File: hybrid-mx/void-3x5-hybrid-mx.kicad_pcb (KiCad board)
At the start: 2 copper layers, 140.5 x 112.5 mm, 81 parts, among them J1 Conn_01x02, J2 Conn_01x03_MountingPin, J3 Conn_01x02

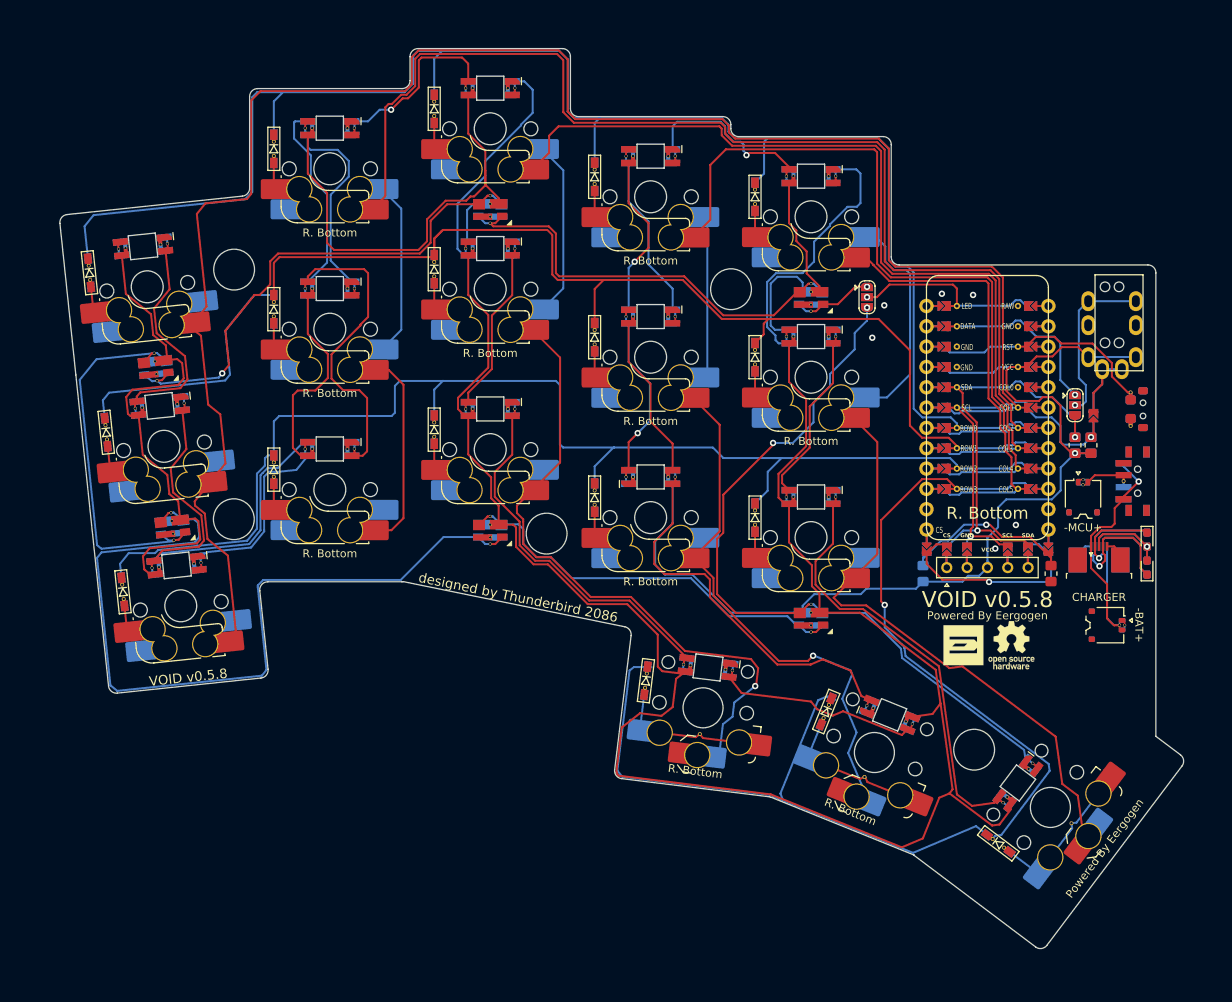
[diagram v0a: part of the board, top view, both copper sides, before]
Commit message: added choc
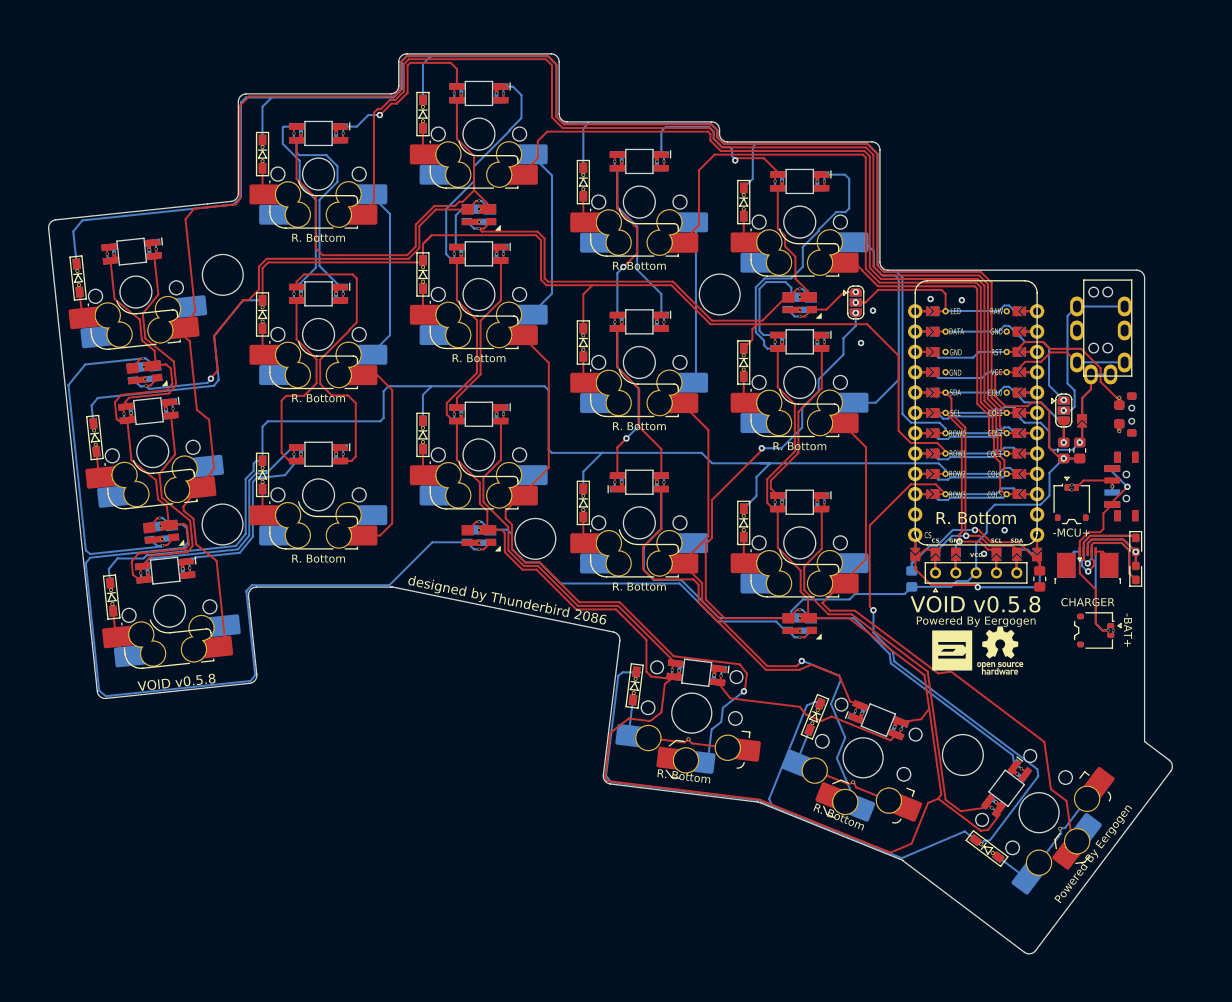
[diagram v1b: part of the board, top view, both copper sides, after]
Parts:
- moved D6 1.56 mm to (107.6, 52.8)
- moved JP1 1.56 mm to (181.8, 71.4)
- moved L12 1.56 mm to (154.7, 53.7)
- moved LED1 1.56 mm to (216.8, 105.2)
- moved LED2 1.56 mm to (216.8, 101.7)
- moved LED3 1.56 mm to (216.8, 105.2)
- moved LED4 1.56 mm to (216.8, 101.7)
- moved S4 1.56 mm to (114.6, 95.4)
- moved JP2 1.56 mm to (207.8, 84.9)
- moved S3 1.56 mm to (91.8, 70.1)
- moved DISP1 1.56 mm to (196.8, 85.2)
- moved LOGO2 1.56 mm to (199.8, 114.9)
- moved MCU1 1.56 mm to (196.8, 85.2)
- moved L17 1.56 mm to (184.6, 123.6)
- moved L23 1.56 mm to (134.7, 100.5)
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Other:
- outline, holes or cut-outs redrawn

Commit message: added holes for oled window
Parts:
- moved LOGO1 3.00 mm to (196.8, 114.9)
- moved LOGO2 3.00 mm to (202.8, 114.9)
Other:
- outline, holes or cut-outs redrawn
- board text added: "VOID v0.5.9"
- board text removed: "VOID v0.5.8"

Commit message: Mcu cover (#7)
* more plates

* updated workflow

* mcu cover

* small change
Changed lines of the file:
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@@
 		(fp_arc
 			(start 4.085177 -6.750222)
-			(mid 5.499395 -6.164435)
+			(mid 5.499391 -6.164435)
 			(end 6.085176 -4.750218)
 			(stroke
@@
 		(fp_arc
 			(start 4.085177 -6.750222)
-			(mid 5.499395 -6.164435)
+			(mid 5.499391 -6.164435)
 			(end 6.085176 -4.750218)
 			(stroke
@@
 		(fp_arc
 			(start 4.085176 -6.750219)
-			(mid 5.499391 -6.164436)
+			(mid 5.499388 -6.164435)
 			(end 6.085177 -4.750222)
 			(stroke
@@
 		(fp_arc
 			(start 4.085176 -6.750219)
-			(mid 5.499391 -6.164436)
+			(mid 5.499388 -6.164435)
 			(end 6.085177 -4.750222)
 			(stroke
@@
 		(fp_arc
 			(start 4.085177 -6.750222)
-			(mid 5.499395 -6.164435)
+			(mid 5.499391 -6.164435)
 			(end 6.085176 -4.750218)
 			(stroke
@@
 		(fp_arc
 			(start 4.085177 -6.750222)
-			(mid 5.499395 -6.164435)
+			(mid 5.499391 -6.164435)
 			(end 6.085176 -4.750218)
 			(stroke
@@
 		(fp_arc
 			(start 4.085177 -6.750222)
-			(mid 5.499395 -6.164435)
+			(mid 5.499391 -6.164435)
 			(end 6.085176 -4.750218)
 			(stroke
@@
 		(fp_arc
 			(start 4.085177 -6.750222)
-			(mid 5.499395 -6.164435)
+			(mid 5.499391 -6.164435)
 			(end 6.085176 -4.750218)
 			(stroke
@@
 		(fp_arc
 			(start 4.085177 -6.750222)
-			(mid 5.499395 -6.164435)
+			(mid 5.499391 -6.164435)
 			(end 6.085176 -4.750218)
 			(stroke
@@
 		(fp_arc
 			(start 4.085177 -6.750222)
-			(mid 5.499395 -6.164435)
+			(mid 5.499391 -6.164435)
 			(end 6.085176 -4.750218)
 			(stroke
@@
 		(fp_arc
 			(start 4.085177 -6.750222)
-			(mid 5.499395 -6.164435)
+			(mid 5.499391 -6.164435)
 			(end 6.085176 -4.750218)
 			(stroke
@@
 		(fp_arc
 			(start 4.085177 -6.750222)
-			(mid 5.499395 -6.164435)
+			(mid 5.499391 -6.164435)
 			(end 6.085176 -4.750218)
 			(stroke
@@
 		(fp_arc
 			(start 4.085177 -6.750222)
-			(mid 5.499395 -6.164435)
+			(mid 5.499391 -6.164435)
 			(end 6.085176 -4.750218)
 			(stroke
@@
 		(fp_arc
 			(start 4.085177 -6.750222)
-			(mid 5.499395 -6.164435)
+			(mid 5.499391 -6.164435)
 			(end 6.085176 -4.750218)
 			(stroke
@@
 		(fp_arc
 			(start 4.085177 -6.750222)
-			(mid 5.499395 -6.164435)
+			(mid 5.499391 -6.164435)
 			(end 6.085176 -4.750218)
 			(stroke
@@
 		(fp_arc
 			(start 4.085177 -6.750222)
-			(mid 5.499395 -6.164435)
+			(mid 5.499391 -6.164435)
 			(end 6.085176 -4.750218)
 			(stroke
@@
 		(fp_arc
 			(start 4.085176 -6.750219)
-			(mid 5.499391 -6.164436)
+			(mid 5.499388 -6.164435)
 			(end 6.085177 -4.750222)
 			(stroke
@@
 		(fp_arc
 			(start 4.085176 -6.750219)
-			(mid 5.499391 -6.164436)
+			(mid 5.499388 -6.164435)
 			(end 6.085177 -4.750222)
 			(stroke
@@
 		(fp_arc
 			(start 4.085177 -6.750222)
-			(mid 5.499395 -6.164435)
+			(mid 5.499391 -6.164435)
 			(end 6.085176 -4.750218)
 			(stroke
@@
 		(fp_arc
 			(start 4.085177 -6.750222)
-			(mid 5.499395 -6.164435)
+			(mid 5.499391 -6.164435)
 			(end 6.085176 -4.750218)
 			(stroke
@@
 		(fp_arc
 			(start 4.085176 -6.750219)
-			(mid 5.499391 -6.164436)
+			(mid 5.499388 -6.164435)
 			(end 6.085177 -4.750222)
 			(stroke
@@
 		(fp_arc
 			(start 4.085176 -6.750219)
-			(mid 5.499391 -6.164436)
+			(mid 5.499388 -6.164435)
 			(end 6.085177 -4.750222)
 			(stroke
@@
 		(fp_arc
 			(start 4.085177 -6.750222)
-			(mid 5.499395 -6.164435)
+			(mid 5.499391 -6.164435)
 			(end 6.085176 -4.750218)
 			(stroke
@@
 		(fp_arc
 			(start 4.085177 -6.750222)
-			(mid 5.499395 -6.164435)
+			(mid 5.499391 -6.164435)
 			(end 6.085176 -4.750218)
 			(stroke
@@
 		(fp_arc
 			(start 4.085177 -6.750222)
-			(mid 5.499395 -6.164435)
+			(mid 5.499391 -6.164435)
 			(end 6.085176 -4.750218)
 			(stroke
@@
 		(fp_arc
 			(start 4.085177 -6.750222)
-			(mid 5.499395 -6.164435)
+			(mid 5.499391 -6.164435)
 			(end 6.085176 -4.750218)
 			(stroke
@@
 		(fp_arc
 			(start 4.085177 -6.750222)
-			(mid 5.499395 -6.164435)
+			(mid 5.499391 -6.164435)
 			(end 6.085176 -4.750218)
 			(stroke
@@
 		(fp_arc
 			(start 4.085177 -6.750222)
-			(mid 5.499395 -6.164435)
+			(mid 5.499391 -6.164435)
 			(end 6.085176 -4.750218)
 			(stroke
@@
 		(fp_arc
 			(start 4.085177 -6.750222)
-			(mid 5.499395 -6.164435)
+			(mid 5.499391 -6.164435)
 			(end 6.085176 -4.750218)
 			(stroke
@@
 		(fp_arc
 			(start 4.085177 -6.750222)
-			(mid 5.499395 -6.164435)
+			(mid 5.499391 -6.164435)
 			(end 6.085176 -4.750218)
 			(stroke

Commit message: fixed bridge for hybrid-mx
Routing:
- net row_thumb: track 160.7 -> 157.2 mm

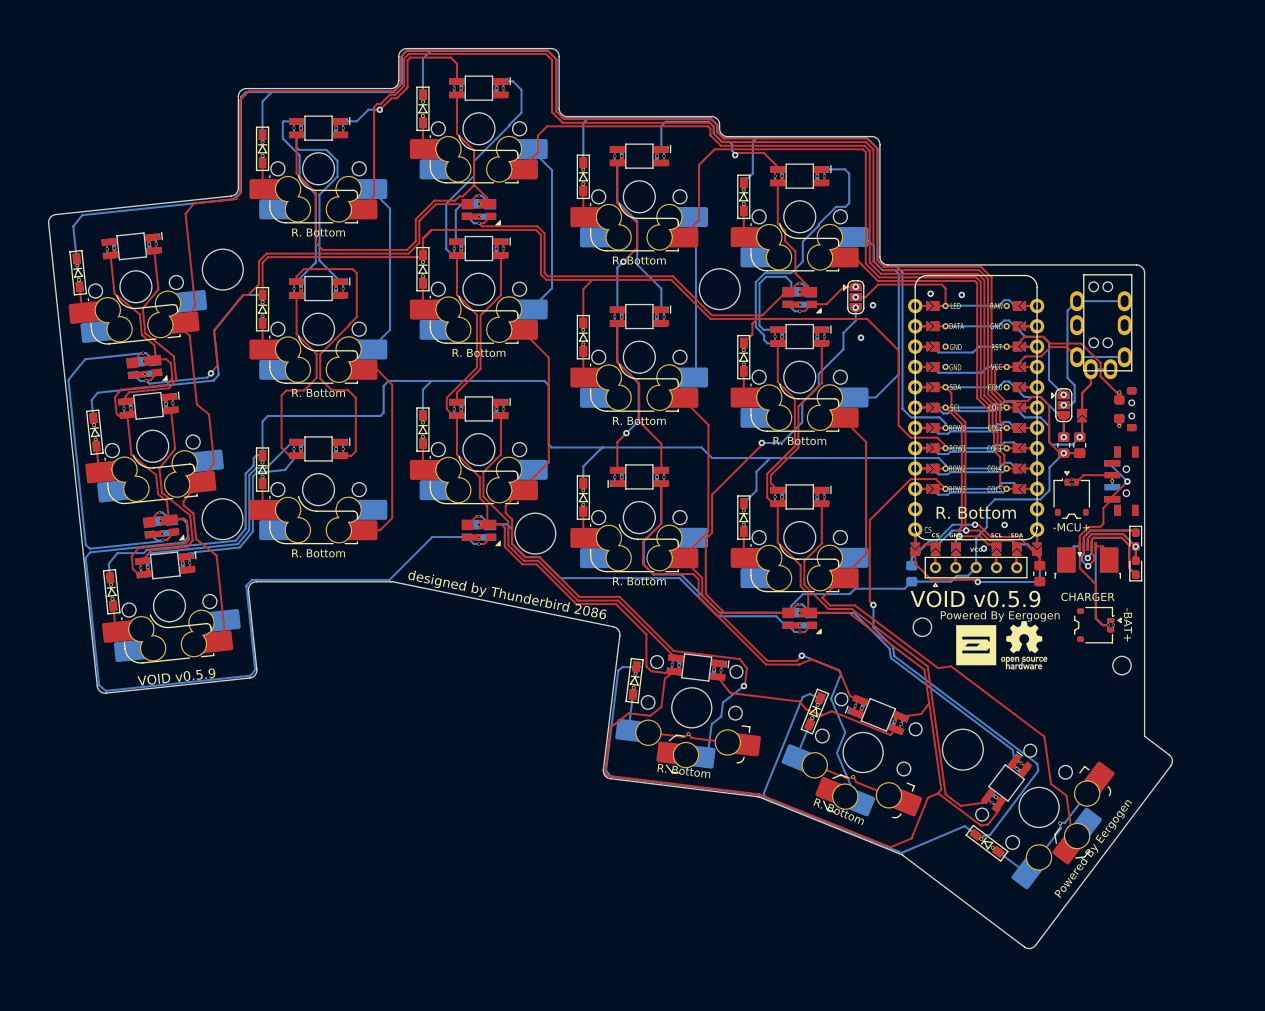
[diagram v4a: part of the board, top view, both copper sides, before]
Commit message: Changed TRRS to USB-C connector (#14)
* usb-c mod for hybrid

* updated
  - submodule
  - ergogen yaml
  - schematic and pcb

* updated cherry-mx

usb-c for communication between left and right hand sides

* updated choc

* updated choc

* fixed corner

* void-choc

* ergogen
  - bottom plate
  - charger plate

* updated choc

* updated ergogen

* cherry-mx
* hybrid-mx

* updated ergogen for VOID Choc

* refreshed submodule

* updated ergogen yaml

* updated PCBs

* updated version
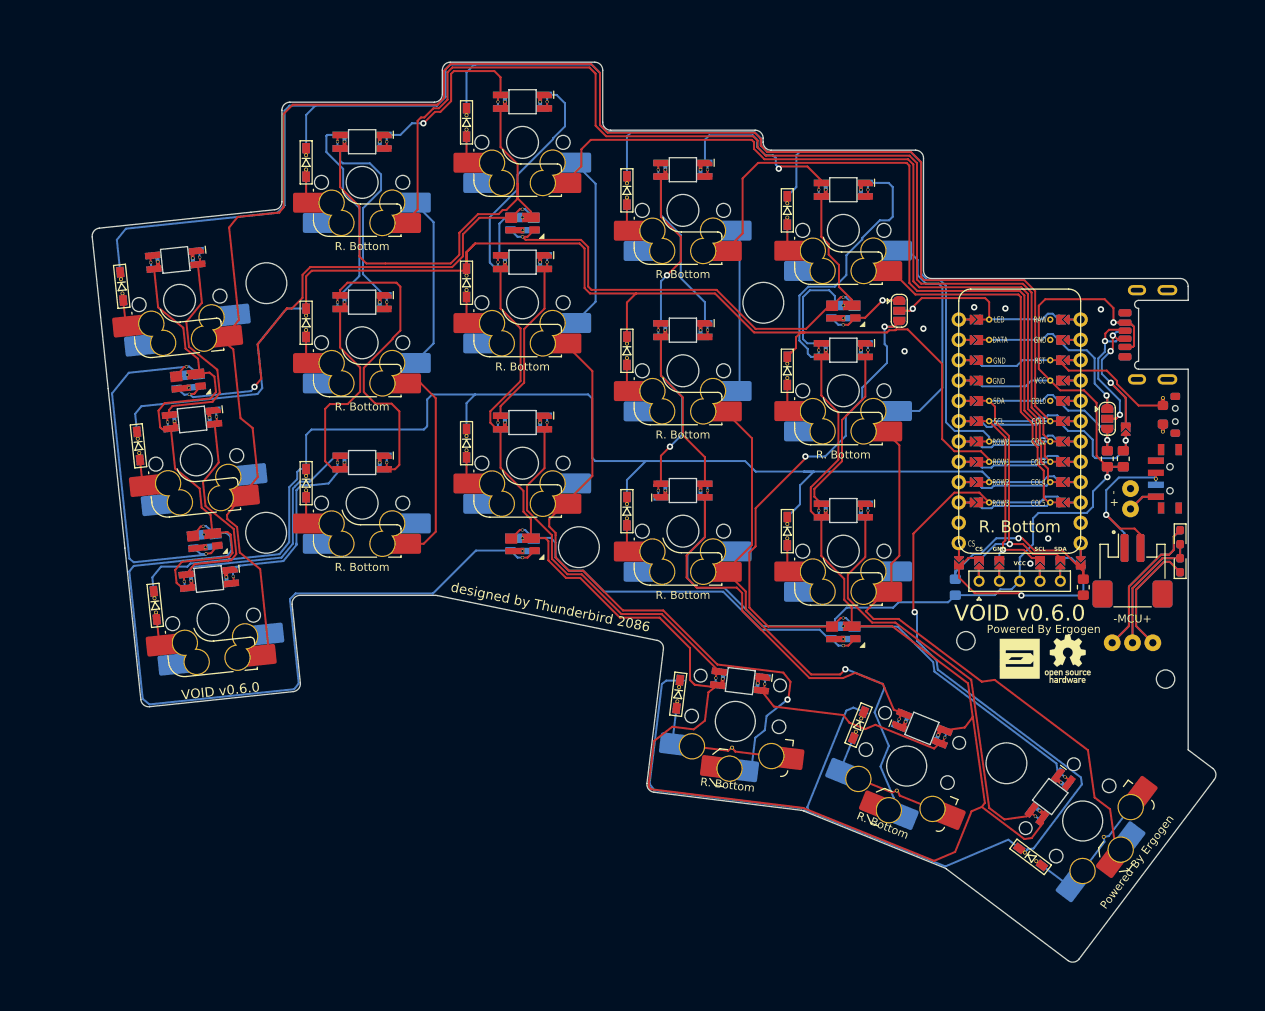
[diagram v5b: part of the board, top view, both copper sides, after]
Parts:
- removed TRRS1: MJ-4PP-9, TB2086_MISC:TRRS-PJ-320A-rev
- added J4: Conn_01x03, TB2086_MISC:Pogopin_1x03_P2.54mm, F.Cu at (216.3, 114.6)
- added SW_SPDT2: SW_SPDT2, TB2086_SMD:SW_SPDT_PCM12, F.Cu at (220.7, 94.1)
- J1: value Conn_01x02 -> USB_C_Receptacle_PowerOnly_6P; footprint TB2086_MISC:Molex_Pico-EZmate_78171-0002_1x02-1MP_P1.20mm_Vertical_rev -> TB2086_SMD:USB-20C-F-6C16_rev
- J2: value Conn_01x03_MountingPin -> Conn_01x02; footprint TB2086_MISC:TE_0-1734839-5_1x05-1MP_P0.5mm_Horizontal-rev -> TB2086_SMD:JST_PH_S2B-PH-SM4-TB_1x02-1MP_P2.00mm_Horizontal_rev
- J3: footprint TB2086_MISC:Molex_Pico-EZmate_78171-0002_1x02-1MP_P1.20mm_Vertical_rev -> TB2086_MISC:Pogopin_1x02_P2.54mm; moved to F.Cu
- L19, L20, L21, L22, L23, L24: footprint LED_SK6812MINI_PLCC4_3.5x3.5mm_P1.75mm_rev_all -> TB2086_LED:LED_SK6812MINI_PLCC4_3.5x3.5mm_P1.75mm_rev_all; moved to F.Cu
- LED1, LED2, LED3, LED4: footprint TB2086_SMD:LED_0603_1608Metric_Pad1.05x0.95mm_HandSolder -> TB2086_LED:LED_0603_1608Metric_Pad1.05x0.95mm_HandSolder
- R1: footprint R_0805_2012Metric_Pad1.20x1.40mm_HandSolder -> Resistor_SMD:R_0805_2012Metric_Pad1.20x1.40mm_HandSolder; moved to B.Cu
- R2: footprint R_0805_2012Metric_Pad1.20x1.40mm_HandSolder -> Resistor_SMD:R_0805_2012Metric_Pad1.20x1.40mm_HandSolder
- S16, S17: value SW_MX_HS -> SW_CHOC_HS
- S18: value SW_MX_HS -> SW_CHOC_HS; footprint TB2086_KEYSWITCH:SW_choc_v1_v2_HS_1.5u_reversible -> TB2086_KEYSWITCH:SW_choc_v1_v2_HS_1u_reversible
- SW_SPDT1: value SW_SPDT -> SW_SPDT1; footprint TB2086_SMD:SW_SPDT_PCM12_reversible -> TB2086_SMD:SW_SPDT_PCM12
- moved J1 23.2 mm to (219.9, 76.1), turned to 90 degrees
- moved J3 16.4 mm to (216.1, 96.6), turned to -90 degrees
- moved LED1 6.72 mm to (222.3, 101.4), turned to -90 degrees
- moved LED4 6.40 mm to (222.3, 104.9)
- moved J2 5.85 mm to (216.3, 105.6)
- moved D15 5.70 mm to (173.2, 60.5)
- moved R4 5.70 mm to (215.2, 91.6)
- moved D14 5.70 mm to (173.2, 80.6)
- moved D18 5.70 mm to (203.6, 141.3)
- moved S12 5.70 mm to (160.1, 60.5)
- moved R1 5.70 mm to (194.2, 107.6)
- moved L11 5.70 mm to (160.1, 75.5)
- moved L9 5.70 mm to (140.1, 46.9)
- moved S7 5.70 mm to (140.1, 92.1)
- moved D2 5.70 mm to (92.1, 89.9)
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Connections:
- J2 pad 1: BAT -> GND
- JP2 pad 2: Net-(JP2-C) -> Net-(J1-CC2)
- JP3 pad 2: Net-(JP3-B) -> Net-(J1-CC1)
- LED1 pad 1: Net-(J2-Pin_4) -> Net-(J4-Pin_1)
- LED1 pad 2: Net-(J2-Pin_3) -> Net-(J4-Pin_2)
- LED2 pad 1: Net-(J2-Pin_4) -> Net-(J4-Pin_1)
- LED2 pad 2: Net-(J2-Pin_3) -> Net-(J4-Pin_2)
- LED3 pad 1: Net-(J2-Pin_2) -> Net-(J4-Pin_3)
- LED3 pad 2: Net-(J2-Pin_3) -> Net-(J4-Pin_2)
- LED4 pad 1: Net-(J2-Pin_2) -> Net-(J4-Pin_3)
- LED4 pad 2: Net-(J2-Pin_3) -> Net-(J4-Pin_2)
- SW_SPDT1 pad 2: Net-(J1-Pin_2) -> Net-(J2-Pin_2)
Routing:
- net Net-(J4-Pin_1): track 0.00 -> 36.4 mm
- net Net-(J4-Pin_2): track 0.00 -> 32.2 mm
- net Net-(J4-Pin_3): track 0.00 -> 30.0 mm
- net BAT: track 37.1 -> 7.60 mm, vias 1 -> 0
- net Net-(J2-Pin_4): track 23.9 -> 0.00 mm, vias 1 -> 0
- net Net-(J1-CC1): track 0.00 -> 22.2 mm, vias 0 -> 3
- net Net-(JP2-C): track 20.9 -> 0.00 mm, vias 1 -> 0
- net Net-(J1-CC2): track 0.00 -> 20.5 mm, vias 0 -> 2
- net Net-(J2-Pin_3): track 19.3 -> 0.00 mm, vias 1 -> 0
- net VCC: track 627.1 -> 642.9 mm, vias 2 -> 3
- net Net-(JP3-B): track 13.8 -> 0.00 mm
- net GND: track 5.73 -> 0.00 mm, vias 6 -> 7
- net Net-(J1-Pin_2): track 4.83 -> 0.00 mm
- net LED_PER_KEY: track 93.4 -> 96.5 mm
- net LED_UNDERGLOW: track 10.1 -> 12.2 mm
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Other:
- outline, holes or cut-outs redrawn
- board text added: "- +"
- board text added: "Powered By Ergogen"
- board text added: "VOID v0.6.0"
- board text added: "offset: 90, 70 from origin"
- board text removed: "-BAT+"
- board text removed: "CHARGER"
- board text removed: "Powered By Eergogen"
- board text removed: "VOID v0.5.9"
